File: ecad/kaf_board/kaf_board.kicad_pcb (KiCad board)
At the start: 2 copper layers, 225 parts, among them J1 Barrel_Jack_Switch, J2 USB_OTG, J3 AUX, J4 Peltier1, J5 Peltier2, M1 Motor_Servo, Q1 MMBT3904LT1G, Q2 NTD4804N, Q3 NTD4804N, U1 MAX4649, U10 LM224, U11 LM224, U12 LM224, U13 LD1117S12CTR_SOT223, U14 LD1117S33CTR_SOT223, U15 LTC3265*FE, U16 93LCxxBxxOT, U17 FT2232H, U18 ICE40HX4K-TQ144, U19 W25X20CL, U2 ADP7118AUJZ, U20 MCP3004, U21 TC4427, U3 AD9826, U4 KAF-CDIP24, U5 TL432LIAIDBZR, U6 TL432LIAIDBZR, U7 TC4427, U8 TC4427, U9 TC4428, Y1 12 MHz

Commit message: continued placing footprints
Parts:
- moved R57 219.3 mm to (26.4, 111.5), turned to 180 degrees
- moved R58 216.4 mm to (26.4, 113.5)
- moved U16 213.4 mm to (51.0, 24.0), turned to 180 degrees
- moved R60 207.2 mm to (19.0, 109.0), turned to 90 degrees
- moved U18 202.8 mm to (49.5, 90.0), turned to 270 degrees
- moved R62 198.0 mm to (30.5, 97.5), turned to 270 degrees
- moved U19 197.6 mm to (26.5, 106.0), turned to 180 degrees
- moved C90 196.7 mm to (26.5, 109.5)
- moved C50 196.2 mm to (85.5, 141.0)
- moved R63 195.6 mm to (31.5, 90.0), turned to 90 degrees
- moved R59 194.4 mm to (26.5, 102.5), turned to 180 degrees
- moved C91 194.1 mm to (37.0, 100.5), turned to 270 degrees
- moved R61 193.6 mm to (32.5, 97.5), turned to 270 degrees
- moved C52 192.4 mm to (85.5, 143.0)
- moved C96 189.6 mm to (33.5, 90.0), turned to 90 degrees
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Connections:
- U9 pad 5: /ccd/H1 -> /ccd/H2
- U9 pad 7: /ccd/H2 -> /ccd/H1

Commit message: added board outline
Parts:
- added H1: MountingHole, Mounting_Holes:MountingHole_4.3mm_M4_ISO7380_Pad, F.Cu at (97.0, 78.5)
- added H2: MountingHole, Mounting_Holes:MountingHole_4.3mm_M4_ISO7380_Pad, F.Cu at (203.0, 126.5)
- added H3: MountingHole, Mounting_Holes:MountingHole_4.3mm_M4_ISO7380_Pad, F.Cu at (97.0, 117.5)
- added H4: MountingHole, Mounting_Holes:MountingHole_4.3mm_M4_ISO7380_Pad, F.Cu at (203.0, 87.5)
- TH1, TH2, TH3: footprint Connectors_JST:JST_SH_BM02B-SRSS-TB_02x1.00mm_Straight -> Connectors:PINHEAD1-2
- moved Q2 521.2 mm to (516.8, 171.8)
- moved L8 518.2 mm to (506.2, 191.8)
- moved C107 515.8 mm to (502.2, 173.8), turned to 270 degrees
- moved L9 515.4 mm to (477.8, 191.8)
- moved Q3 508.2 mm to (488.4, 172.0)
- moved C108 501.1 mm to (474.2, 174.8), turned to 270 degrees
- moved C105 495.9 mm to (492.2, 160.2), turned to 90 degrees
- moved D4 494.8 mm to (504.8, 167.8)
- moved U21 490.9 mm to (497.2, 160.2), turned to 270 degrees
- moved J4 490.5 mm to (497.2, 172.7), turned to 270 degrees
- moved D5 476.5 mm to (475.8, 168.2)
- moved C106 475.0 mm to (494.2, 160.2), turned to 90 degrees
- moved J5 462.3 mm to (468.8, 173.8), turned to 270 degrees
- moved R44 435.8 mm to (531.8, 22.8), turned to 180 degrees
- moved C60 422.3 mm to (532.2, 39.8), turned to 180 degrees
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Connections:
- U15 pad 1: (no net) -> Net-(C59-Pad2)
- U15 pad 11: (no net) -> Net-(C55-Pad1)
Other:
- board outline added: 116 x 71 mm
- copper layers 2 -> 4
- net class High current added: clearance 0.2, trace_width 0.5, via_dia 0.8, via_drill 0.4
- net class Power added: clearance 0.2, trace_width 0.5, via_dia 0.8, via_drill 0.4
- board text added: "CUT OUT"

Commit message: continued footprint placement
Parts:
- added M2: Servo cut-out, kaf_board:HD-1440A, F.Cu at (166.2, 59.2)
- C21, C24, C41, C42, C43, C44, C45, C46, C47, C48, C49, C50, C51, C52, C53, C54, C55, C56, C59, C62, C63, C64, C65, R10, R11, R20, R21, R22, R23, R24, R25, R26, R27, R28, R29, R30, R31, R32, R33, R34, R35, R36, R37, R38, R39, R4, R40, R41, R42, R43, R45, R46, R47, R48, R5, R6, R9, U10, U11, U12, U15, U5, U6: moved to B.Cu
- moved C57 456.4 mm to (78.2, 94.2)
- moved C58 456.4 mm to (78.8, 109.2)
- moved C60 456.4 mm to (79.8, 99.2)
- moved C61 456.4 mm to (79.2, 84.2)
- moved R44 456.4 mm to (79.2, 82.2)
- moved U13 456.4 mm to (79.2, 89.2)
- moved U14 456.4 mm to (79.8, 104.5)
- moved J3 342.4 mm to (84.0, 152.5), turned to 0 degrees
- moved C102 330.1 mm to (32.8, 34.8)
- moved C103 330.1 mm to (20.5, 31.0)
- moved C66 330.1 mm to (85.5, 33.3)
- moved C67 330.1 mm to (75.5, 23.3)
- moved C68 330.1 mm to (80.9, 33.3)
- moved C69 330.1 mm to (61.1, 38.1)
- moved F1 330.1 mm to (84.0, 23.7)
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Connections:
- C14 pad 1: /ccd/ccd_voltage_1/V1 -> /ccd/VGUARD
- U1 pad 8: /ccd/V_AMPL -> (no net)
- U10 pad 1: /ccd/ccd_voltage_1/V1 -> /ccd/V_AMP
- U10 pad 2: /ccd/ccd_voltage_1/V1 -> /ccd/V_AMP
- U11 pad 13: /ccd/V_AMPL -> /ccd/VGUARD
- U11 pad 14: /ccd/V_AMPL -> /ccd/VGUARD
- U4 pad 23: /ccd/ccd_voltage_1/V1 -> /ccd/VGUARD
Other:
- outline, holes or cut-outs redrawn

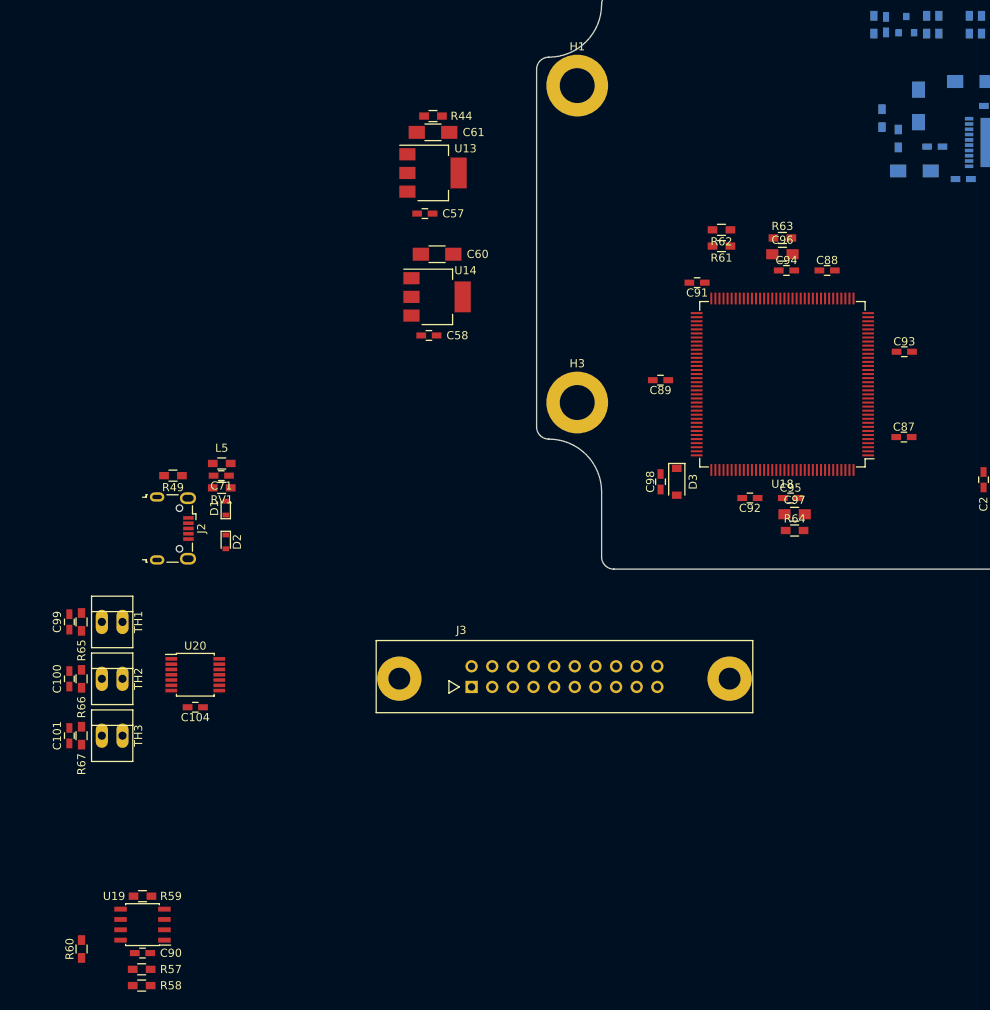
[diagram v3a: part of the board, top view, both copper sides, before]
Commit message: changes schematics and PCB to ice40hx1k-vq100
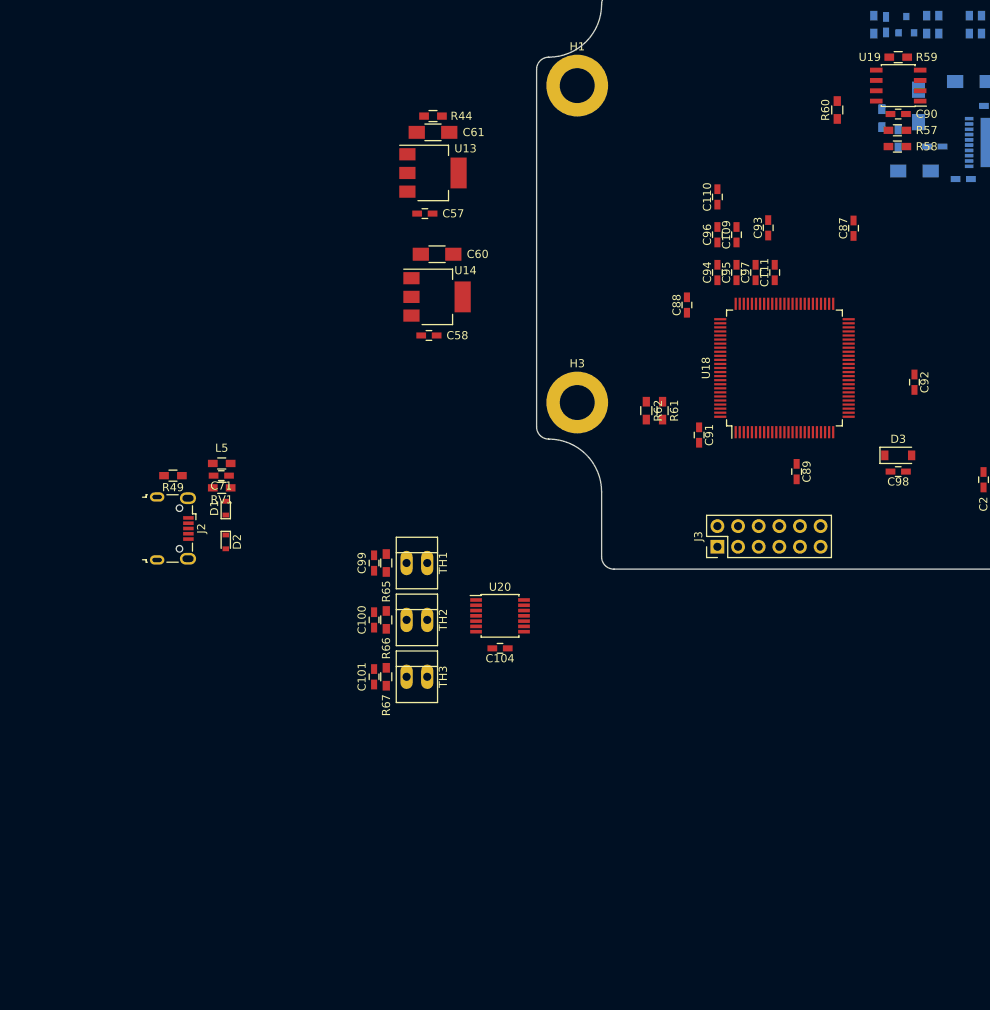
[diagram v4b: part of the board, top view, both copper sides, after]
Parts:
- removed R63, R64: 100, Resistors_SMD:R_0603_HandSoldering
- added C109: 0.1u, Capacitors_SMD:C_0603_HandSoldering, F.Cu at (116.6, 96.8)
- added C110: 0.1u, Capacitors_SMD:C_0603_HandSoldering, F.Cu at (114.2, 92.2)
- added C111: 0.1u, Capacitors_SMD:C_0603_HandSoldering, F.Cu at (121.3, 101.5)
- C96, C97: value 10u -> 0.1u; footprint Capacitors_SMD:C_0805_HandSoldering -> Capacitors_SMD:C_0603_HandSoldering
- J3: footprint Connectors:HE10-20D -> Pin_Headers:Pin_Header_Straight_2x06_Pitch2.54mm
- R62: value need to calc -> 2.2k
- U18: value ICE40HX4K-TQ144 -> ICE40HX1K-VQ100; footprint Housings_QFP:TQFP-144_20x20mm_Pitch0.5mm -> Housings_QFP:LQFP-100_14x14mm_Pitch0.5mm
- moved C90 139.0 mm to (136.5, 82.0)
- moved R57 139.0 mm to (136.4, 84.0)
- moved R58 139.0 mm to (136.4, 86.0)
- moved R59 139.0 mm to (136.5, 75.0)
- moved R60 139.0 mm to (129.0, 81.5)
- moved U19 139.0 mm to (136.5, 78.5)
- moved C100 38.2 mm to (72.0, 144.2)
- moved C101 38.2 mm to (72.0, 151.2)
- moved C104 38.2 mm to (87.5, 147.8)
- moved C99 38.2 mm to (72.0, 137.2)
- moved R65 38.2 mm to (73.5, 137.2)
- moved R66 38.2 mm to (73.5, 144.2)
- moved R67 38.2 mm to (73.5, 151.2)
- moved TH1 38.2 mm to (76.0, 137.2)
- moved TH2 38.2 mm to (76.0, 144.2)
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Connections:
- C88 pad 1: +3V3 -> +1V2
- C93 pad 1: +1V2 -> +3V3
- C94 pad 1: /fpga/VCCPLL0 -> +1V2
- C94 pad 2: Net-(C94-Pad2) -> GND
- C95 pad 1: /fpga/VCCPLL1 -> +3V3
- C95 pad 2: Net-(C95-Pad2) -> GND
- C96 pad 1: /fpga/VCCPLL0 -> +3V3
- C96 pad 2: Net-(C94-Pad2) -> GND
- C97 pad 1: /fpga/VCCPLL1 -> +3V3
- C97 pad 2: Net-(C95-Pad2) -> GND
- J3 pad 1: Net-(J3-Pad1) -> /fpga/AUX1
- J3 pad 10: Net-(J3-Pad10) -> /fpga/AUX10
- J3 pad 11: Net-(J3-Pad11) -> /fpga/AUX11
- J3 pad 12: Net-(J3-Pad12) -> /fpga/AUX12
- J3 pad 2: Net-(J3-Pad2) -> /fpga/AUX2
- J3 pad 3: Net-(J3-Pad3) -> /fpga/AUX3
- J3 pad 4: Net-(J3-Pad4) -> /fpga/AUX4
- J3 pad 5: Net-(J3-Pad5) -> /fpga/AUX5
- J3 pad 6: Net-(J3-Pad6) -> /fpga/AUX6
- J3 pad 7: Net-(J3-Pad7) -> /fpga/AUX6
- J3 pad 8: Net-(J3-Pad8) -> /fpga/AUX8
- J3 pad 9: Net-(J3-Pad9) -> /fpga/AUX9
- R61 pad 1: /usb-interface/FT_CRESET -> +3V3
- R61 pad 2: +3V3 -> /usb-interface/FT_CRESET
- R62 pad 1: /usb-interface/FT_CDONE -> +3V3
- R62 pad 2: +3V3 -> /usb-interface/FT_CDONE
- U18 pad 1: /fpga/FT_OE# -> /fpga/AUX1
- U18 pad 10: /fpga/FT_D7 -> /fpga/AUX8
- U18 pad 100: +3V3 -> /fpga/PWM_SERVO
- U18 pad 11: /fpga/FT_D6 -> +1V2
- U18 pad 12: /fpga/FT_D5 -> /fpga/AUX9
- U18 pad 13: GND -> /fpga/AUX10
- U18 pad 14: GND -> +3V3
- U18 pad 15: /fpga/FT_D4 -> /fpga/AUX11
- U18 pad 16: /fpga/FT_D3 -> /fpga/AUX12
- U18 pad 17: /fpga/FT_D2 -> GND
- U18 pad 18: /fpga/FT_D1 -> /ccd/AMP_OFF
- U18 pad 19: /fpga/FT_D0 -> /ccd/H_3.3V
- U18 pad 2: /fpga/FT_CLKOUT -> /fpga/AUX2
- U18 pad 20: /ccd/AD_D0 -> /ccd/R_3.3V
- U18 pad 21: /ccd/AD_D1 -> /ccd/AD_SLOAD
- U18 pad 22: /ccd/AD_D2 -> +3V3
- U18 pad 23: /ccd/AD_D3 -> GND
- U18 pad 24: /ccd/AD_D4 -> /ccd/AD_SCLK
- U18 pad 25: /ccd/AD_D5 -> /ccd/AD_SDATA
- U18 pad 26: /ccd/AD_D6 -> /ccd/AD_D0
- U18 pad 27: +1V2 -> /ccd/AD_D1
- U18 pad 28: /ccd/AD_D7 -> /ccd/AD_D2
- U18 pad 29: (no net) -> /ccd/AD_D3
- U18 pad 3: /fpga/FT_SIWUA -> /fpga/AUX3
- U18 pad 30: +3V3 -> /ccd/AD_D4
- U18 pad 31: /ccd/AD_OEB -> +3V3
- U18 pad 32: /ccd/AD_CDSCLK1 -> GND
- U18 pad 33: /ccd/AD_CDSCLK2 -> /ccd/AD_D5
- U18 pad 34: /ccd/AD_ADCLK -> /ccd/AD_D6
- U18 pad 35: (no net) -> +1V2
- U18 pad 36: (no net) -> /ccd/AD_D7
- U18 pad 37: /ccd/AD_SDATA -> /ccd/AD_OEB
- U18 pad 38: /ccd/AD_SCLK -> +3V3
- U18 pad 39: /ccd/AD_SLOAD -> GND
- U18 pad 4: /fpga/FT_WR# -> /fpga/AUX4
- U18 pad 40: +1V2 -> /ccd/AD_CDSCLK1
- U18 pad 41: (no net) -> /ccd/AD_CDSCLK2
- U18 pad 42: (no net) -> /ccd/AD_ADCLK
- U18 pad 43: /fpga/MCP_CS_N -> /usb-interface/FT_CDONE
- U18 pad 44: /fpga/MCP_DIN -> /usb-interface/FT_CRESET
- U18 pad 45: /fpga/MCP_DOUT -> /usb-interface/FT_MOSI
- U18 pad 46: +3V3 -> /usb-interface/FT_MISO
- U18 pad 47: /fpga/MCP_CLK -> GND
- U18 pad 48: (no net) -> /usb-interface/FT_SCK
- U18 pad 49: (no net) -> /usb-interface/FT_SS
- U18 pad 50: (no net) -> +3V3
- U18 pad 53: Net-(C94-Pad2) -> (no net)
- U18 pad 54: /fpga/VCCPLL0 -> /fpga/FT_OE#
- U18 pad 55: /ccd/AMP_OFF -> GND
- U18 pad 56: /ccd/H_3.3V -> /fpga/FT_CLKOUT
- U18 pad 57: +3V3 -> /fpga/FT_SIWUA
- U18 pad 58: (no net) -> +3V3
- U18 pad 59: GND -> /fpga/FT_WR#
- U18 pad 60: /ccd/R_3.3V -> /fpga/FT_RD#
- U18 pad 61: /fpga/V1_3.3V -> +1V2
- U18 pad 62: /ccd/V1_3.3V -> /fpga/FT_TXE#
- U18 pad 63: (no net) -> /fpga/FT_RXF#
- U18 pad 65: /usb-interface/FT_CDONE -> /fpga/FT_D7
- U18 pad 66: /usb-interface/FT_CRESET -> /fpga/FT_D6
- U18 pad 67: /usb-interface/FT_MOSI -> +3V3
- U18 pad 68: /usb-interface/FT_MISO -> /fpga/FT_D5
- U18 pad 69: GND -> /fpga/FT_D4
- U18 pad 7: /fpga/FT_RD# -> /fpga/AUX5
- U18 pad 70: /usb-interface/FT_SCK -> GND
- U18 pad 71: /usb-interface/FT_SS -> /fpga/FT_D3
- U18 pad 72: +3V3 -> /fpga/FT_D2
- U18 pad 73: /fpga/PWM_TEC1 -> /fpga/FT_D1
- U18 pad 74: GND -> /fpga/FT_D0
- U18 pad 75: /fpga/PWM_SERVO -> Net-(D3-Pad1)
- U18 pad 77: (no net) -> +1V2
- U18 pad 78: (no net) -> /fpga/V1_3.3V
- U18 pad 79: (no net) -> /ccd/V1_3.3V
- U18 pad 8: /fpga/FT_TXE# -> /fpga/AUX6
- U18 pad 84: (no net) -> GND
- U18 pad 86: GND -> (no net)
- U18 pad 88: (no net) -> +3V3
- U18 pad 89: +3V3 -> (no net)
- U18 pad 9: /fpga/FT_RXF# -> (no net)
- U18 pad 91: (no net) -> /fpga/MCP_CS_N
- U18 pad 92: +1V2 -> +3V3
- U18 pad 93: (no net) -> /fpga/MCP_DIN
- U18 pad 94: (no net) -> /fpga/MCP_DOUT
- U18 pad 95: (no net) -> /fpga/MCP_CLK
- U18 pad 97: (no net) -> /fpga/PWM_TEC1
- U18 pad 98: (no net) -> GND
- U18 pad 99: (no net) -> GND

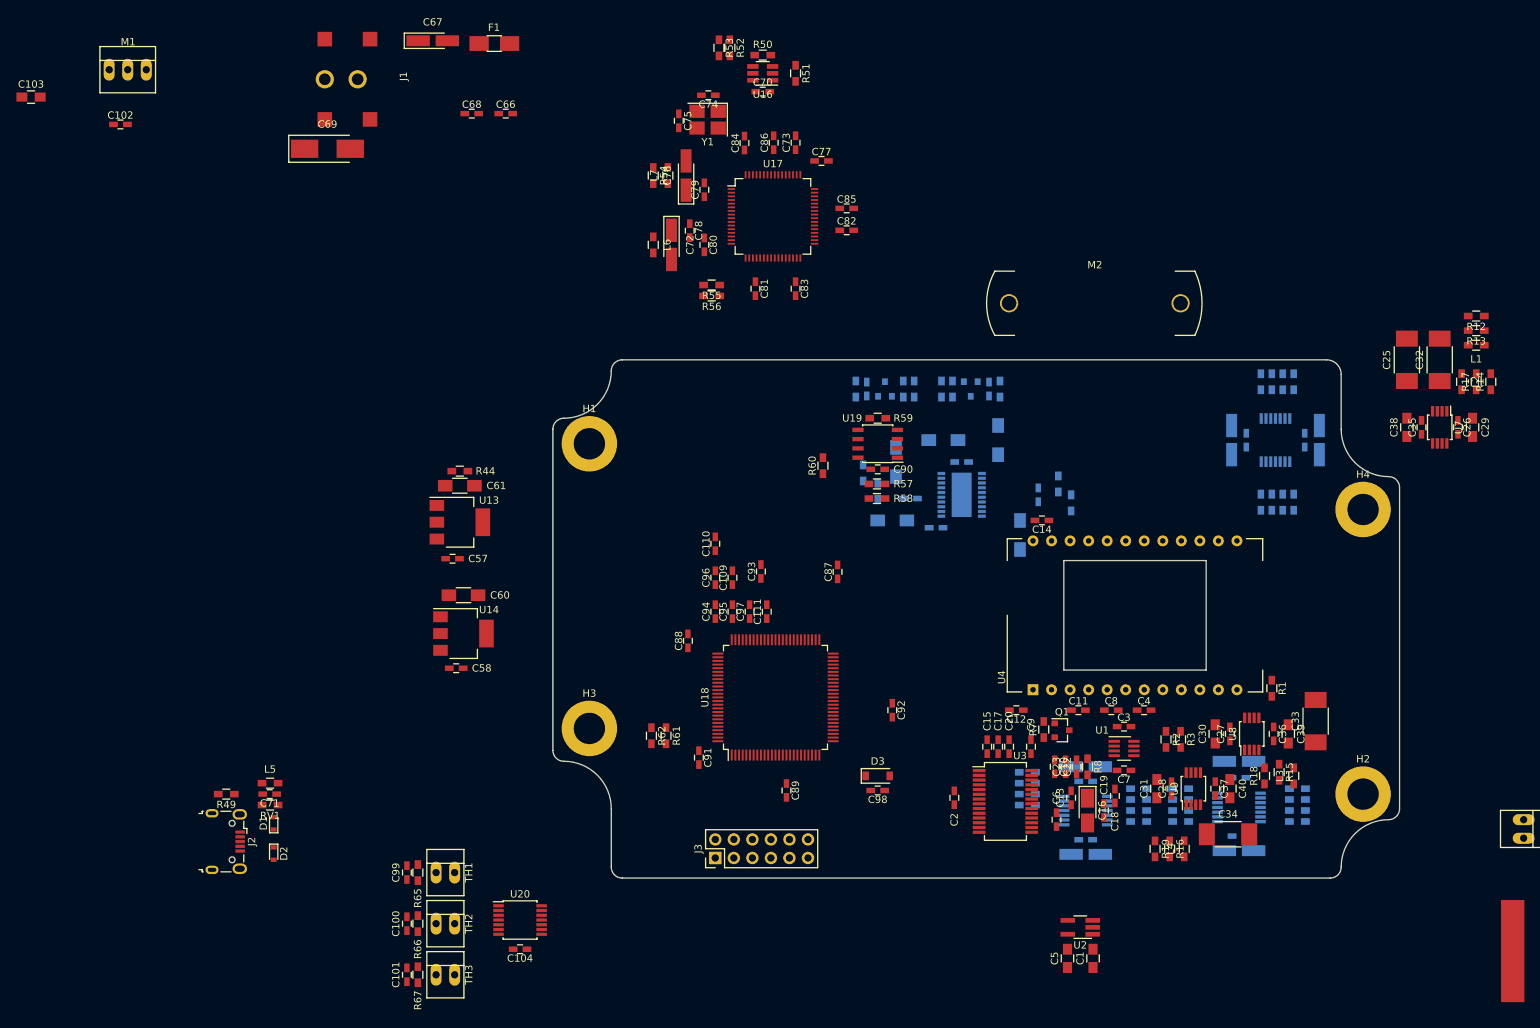
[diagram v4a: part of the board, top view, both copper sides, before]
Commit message: added oscillator to fpga. footprint placement
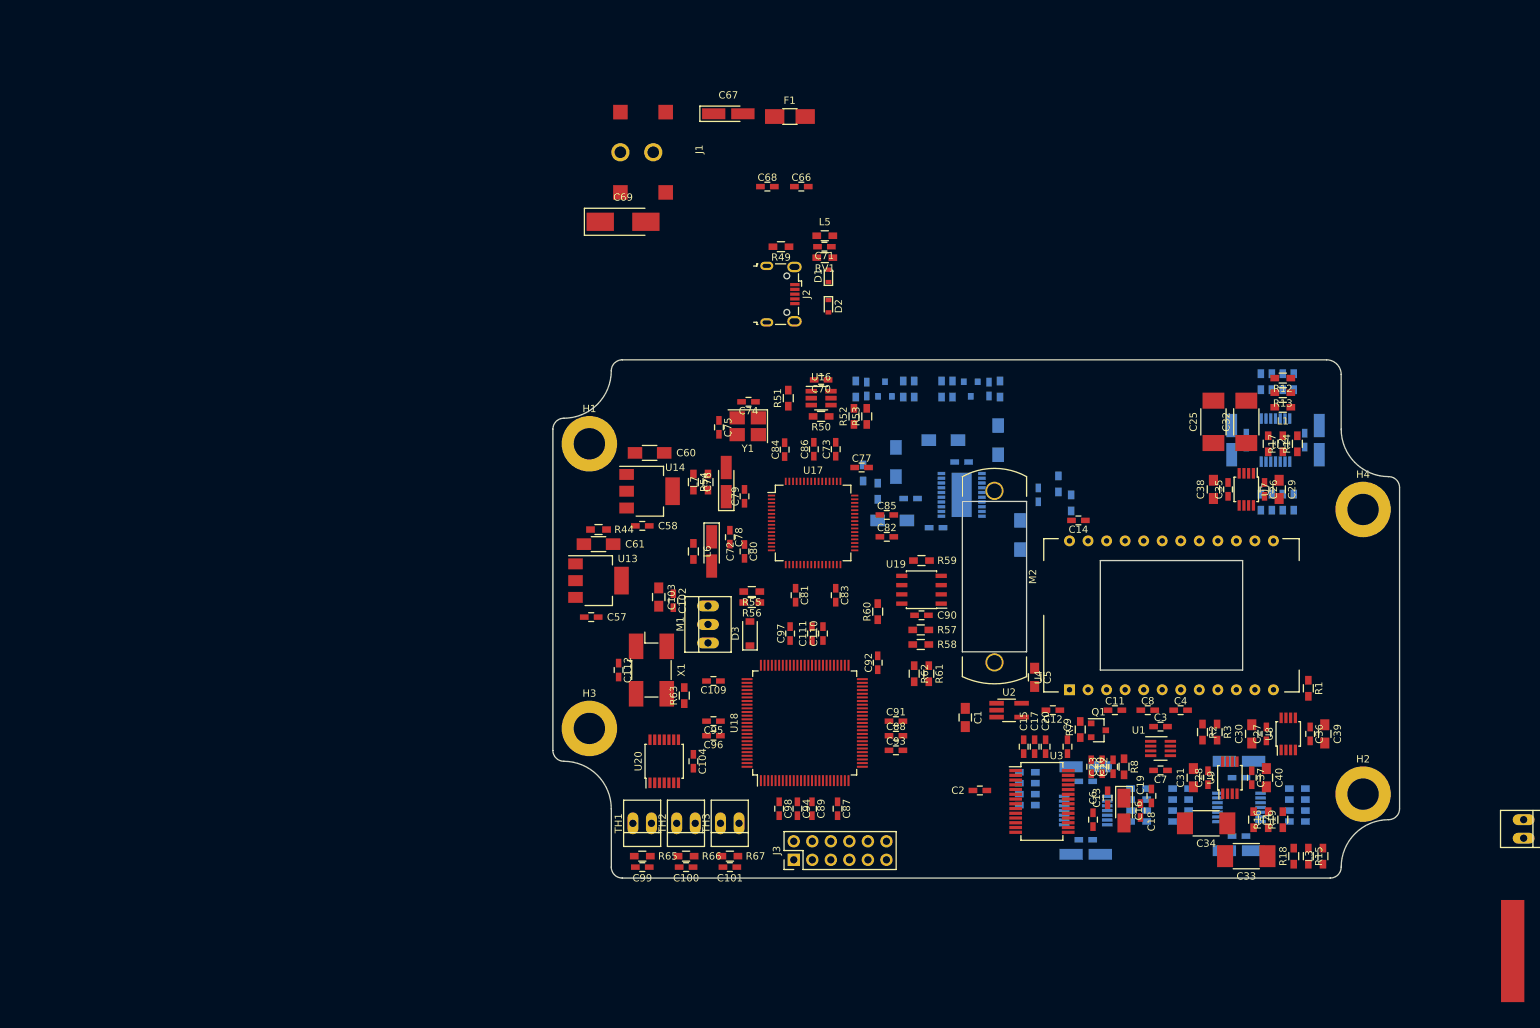
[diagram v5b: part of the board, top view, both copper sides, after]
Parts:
- added C112: C, Capacitors_SMD:C_0603_HandSoldering, F.Cu at (101.0, 109.5)
- added R63: R22, Resistors_SMD:R_0603_HandSoldering, F.Cu at (110.0, 113.0)
- added X1: KC7050A-C3, Oscillators:Oscillator_SMD_EuroQuartz_XO91-4pin_7.0x5.0mm_HandSoldering, F.Cu at (105.5, 109.5)
- moved M1 113.6 mm to (113.2, 105.8), turned to 90 degrees
- moved C103 109.9 mm to (106.5, 99.5), turned to 270 degrees
- moved D1 106.8 mm to (129.8, 55.5)
- moved D2 106.8 mm to (129.8, 59.6)
- moved J2 106.8 mm to (123.2, 58.0)
- moved L5 106.8 mm to (129.2, 50.0)
- moved R49 106.8 mm to (123.2, 51.5)
- moved RV1 106.8 mm to (129.2, 53.0)
- moved C71 106.8 mm to (129.2, 51.5)
- moved C102 100.0 mm to (108.5, 100.0), turned to 270 degrees
- moved R53 54.4 mm to (135.0, 74.8), turned to 90 degrees
- moved R52 53.3 mm to (133.2, 74.8), turned to 90 degrees
- moved R50 50.1 mm to (128.8, 74.8), turned to 180 degrees
- moved C101 46.6 mm to (116.2, 136.5), turned to 180 degrees
- moved TH3 46.4 mm to (117.5, 130.5), turned to 180 degrees
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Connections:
- U18 pad 52: (no net) -> /fpga/FT_OE#
- U18 pad 53: (no net) -> /fpga/FT_CLKOUT
- U18 pad 54: /fpga/FT_OE# -> /fpga/FT_SIWUA
- U18 pad 56: /fpga/FT_CLKOUT -> /fpga/FT_WR#
- U18 pad 57: /fpga/FT_SIWUA -> /fpga/FT_RD#
- U18 pad 59: /fpga/FT_WR# -> /fpga/FT_TXE#
- U18 pad 60: /fpga/FT_RD# -> /fpga/FT_RXF#
- U18 pad 62: /fpga/FT_TXE# -> (no net)
- U18 pad 63: /fpga/FT_RXF# -> (no net)
- U18 pad 90: (no net) -> /fpga/CLK
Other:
- outline, holes or cut-outs redrawn
